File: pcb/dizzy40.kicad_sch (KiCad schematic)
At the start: 102 parts, among them U1 ATmega32U2-A, U2 SRV05-4, X1 Crystal_GND24_Small

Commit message: finalize fab version
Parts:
- RGB1, RGB2, RGB3, RGB4, RGB5, RGB6, RGB7, RGB8: LCSC (none) -> C965556
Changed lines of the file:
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@@
       (effects (font (size 1.27 1.27)) (justify left top) hide)
+    )
+    (property "LCSC" "C965556" (id 4) (at 152.4 139.7 0)
+      (effects (font (size 1.27 1.27)) hide)
     )
     (pin "1")
@@
       (effects (font (size 1.27 1.27)) (justify left top) hide)
     )
+    (property "LCSC" "C965556" (id 4) (at 228.6 139.7 0)
+      (effects (font (size 1.27 1.27)) hide)
+    )
     (pin "1")
     (pin "2")
@@
       (effects (font (size 1.27 1.27)) (justify left top) hide)
     )
+    (property "LCSC" "C965556" (id 4) (at 213.36 139.7 0)
+      (effects (font (size 1.27 1.27)) hide)
+    )
     (pin "1")
     (pin "2")
@@
       (effects (font (size 1.27 1.27)) (justify left top) hide)
     )
+    (property "LCSC" "C965556" (id 4) (at 167.64 139.7 0)
+      (effects (font (size 1.27 1.27)) hide)
+    )
     (pin "1")
     (pin "2")
@@
       (effects (font (size 1.27 1.27)) (justify left top) hide)
     )
+    (property "LCSC" "C965556" (id 4) (at 243.84 139.7 0)
+      (effects (font (size 1.27 1.27)) hide)
+    )
     (pin "1")
     (pin "2")
@@
       (effects (font (size 1.27 1.27)) (justify left top) hide)
     )
+    (property "LCSC" "C965556" (id 4) (at 182.88 139.7 0)
+      (effects (font (size 1.27 1.27)) hide)
+    )
     (pin "1")
     (pin "2")
@@
       (effects (font (size 1.27 1.27)) (justify left top) hide)
     )
+    (property "LCSC" "C965556" (id 4) (at 198.12 139.7 0)
+      (effects (font (size 1.27 1.27)) hide)
+    )
     (pin "1")
     (pin "2")
@@
       (effects (font (size 1.27 1.27)) (justify left top) hide)
     )
-    (pin "1")
+    (property "LCSC" "C965556" (id 4) (at 259.08 139.7 0)
+      (effects (font (size 1.27 1.27)) hide)
+    )
+    (pin "1")

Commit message: update LED part number
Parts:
- RGB1, RGB2, RGB3, RGB4, RGB5, RGB6, RGB7, RGB8: LCSC C965556 -> C965555
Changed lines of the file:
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@@
       (effects (font (size 1.27 1.27)) (justify left top) hide)
     )
-    (property "LCSC" "C965556" (id 4) (at 152.4 139.7 0)
+    (property "LCSC" "C965555" (id 4) (at 152.4 139.7 0)
       (effects (font (size 1.27 1.27)) hide)
     )
@@
       (effects (font (size 1.27 1.27)) (justify left top) hide)
     )
-    (property "LCSC" "C965556" (id 4) (at 228.6 139.7 0)
+    (property "LCSC" "C965555" (id 4) (at 228.6 139.7 0)
       (effects (font (size 1.27 1.27)) hide)
     )
@@
       (effects (font (size 1.27 1.27)) (justify left top) hide)
     )
-    (property "LCSC" "C965556" (id 4) (at 213.36 139.7 0)
+    (property "LCSC" "C965555" (id 4) (at 213.36 139.7 0)
       (effects (font (size 1.27 1.27)) hide)
     )
@@
       (effects (font (size 1.27 1.27)) (justify left top) hide)
     )
-    (property "LCSC" "C965556" (id 4) (at 167.64 139.7 0)
+    (property "LCSC" "C965555" (id 4) (at 167.64 139.7 0)
       (effects (font (size 1.27 1.27)) hide)
     )
@@
       (effects (font (size 1.27 1.27)) (justify left top) hide)
     )
-    (property "LCSC" "C965556" (id 4) (at 243.84 139.7 0)
+    (property "LCSC" "C965555" (id 4) (at 243.84 139.7 0)
       (effects (font (size 1.27 1.27)) hide)
     )
@@
       (effects (font (size 1.27 1.27)) (justify left top) hide)
     )
-    (property "LCSC" "C965556" (id 4) (at 182.88 139.7 0)
+    (property "LCSC" "C965555" (id 4) (at 182.88 139.7 0)
       (effects (font (size 1.27 1.27)) hide)
     )
@@
       (effects (font (size 1.27 1.27)) (justify left top) hide)
     )
-    (property "LCSC" "C965556" (id 4) (at 198.12 139.7 0)
+    (property "LCSC" "C965555" (id 4) (at 198.12 139.7 0)
       (effects (font (size 1.27 1.27)) hide)
     )
@@
       (effects (font (size 1.27 1.27)) (justify left top) hide)
     )
-    (property "LCSC" "C965556" (id 4) (at 259.08 139.7 0)
-      (effects (font (size 1.27 1.27)) hide)
-    )
+    (property "LCSC" "C965555" (id 4) (at 259.08 139.7 0)
+      (effects (font (size 1.27 1.27)) hide)
+    )

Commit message: outline for updated project
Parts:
- removed C1: 10uF, Capacitor_SMD:C_0805_2012Metric, symbol Device:C_Small
- removed C2, C3: 0.1uF, Capacitor_SMD:C_0805_2012Metric, symbol Device:C_Small
- removed C4, C5: 22pF, Capacitor_SMD:C_0805_2012Metric, symbol Device:C_Small
- removed C6: 1uF, Capacitor_SMD:C_0805_2012Metric, symbol Device:C_Small
- removed F1: Polyfuse_Small, Fuse:Fuse_1206_3216Metric, symbol Device:Polyfuse_Small
- removed R1, R2: 5.1k, Resistor_SMD:R_0805_2012Metric, symbol Device:R_Small
- removed R3, R4: 22, Resistor_SMD:R_0805_2012Metric, symbol Device:R_Small
- removed R5, R6: 10k, Resistor_SMD:R_0805_2012Metric, symbol Device:R_Small
- removed RESET1: RESET, Connector_PinHeader_2.54mm:PinHeader_1x02_P2.54mm_Vertical, symbol Switch:SW_Push
- removed U1: ATmega32U2-A, Package_QFP:TQFP-32_7x7mm_P0.8mm, symbol MCU_Microchip_ATmega:ATmega32U2-A
- removed U2: SRV05-4, Package_TO_SOT_SMD:SOT-23-6, symbol Power_Protection:SRV05-4
- removed USB1: USB_C_Receptacle_USB2.0, Connector_USB:USB_C_Receptacle_HRO_TYPE-C-31-M-12, symbol Connector:USB_C_Receptacle_USB2.0
- removed X1: Crystal_GND24_Small, Crystal:Crystal_SMD_3225-4Pin_3.2x2.5mm, symbol Device:Crystal_GND24_Small
- added SW1, SW2: RotaryEncoder_Switch, symbol Device:RotaryEncoder_Switch
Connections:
- net GND: now also SW1.C, SW2.C
- new net ENC_ESC_L: SW1.A
- new net ENC_ESC_R: SW1.B
- new net ENC_SPC_L: SW2.A
- new net ENC_SPC_R: SW2.B
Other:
- added sheet MCU (../../Clacky40/pcb/rp2040/RP2040_tmp.kicad_sch)

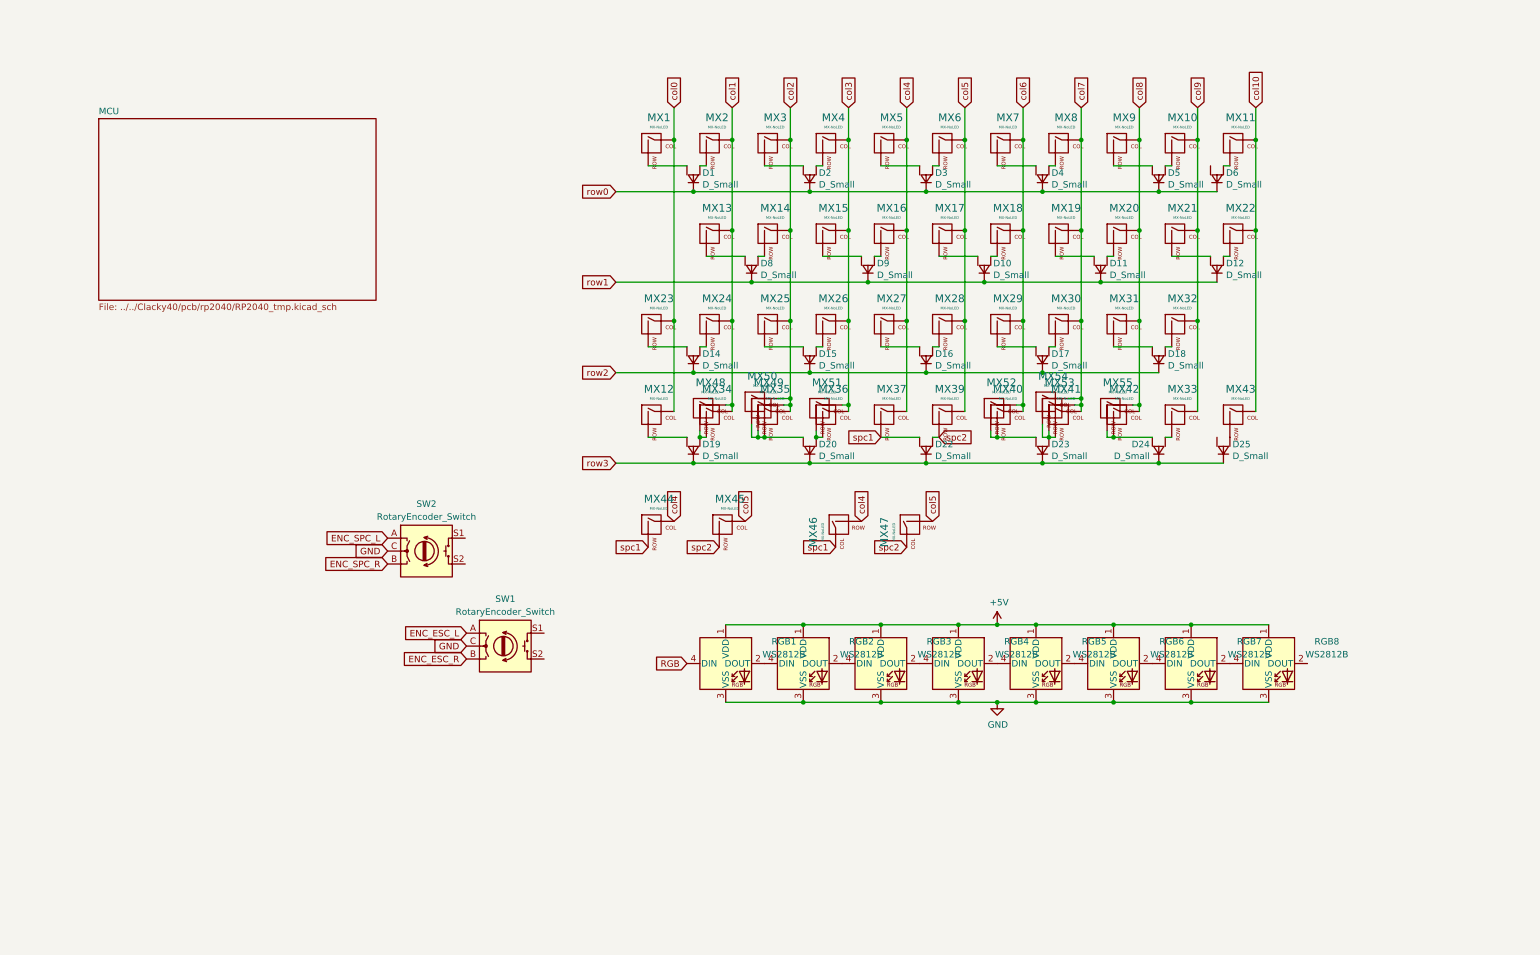
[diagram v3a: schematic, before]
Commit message: diode positioning done
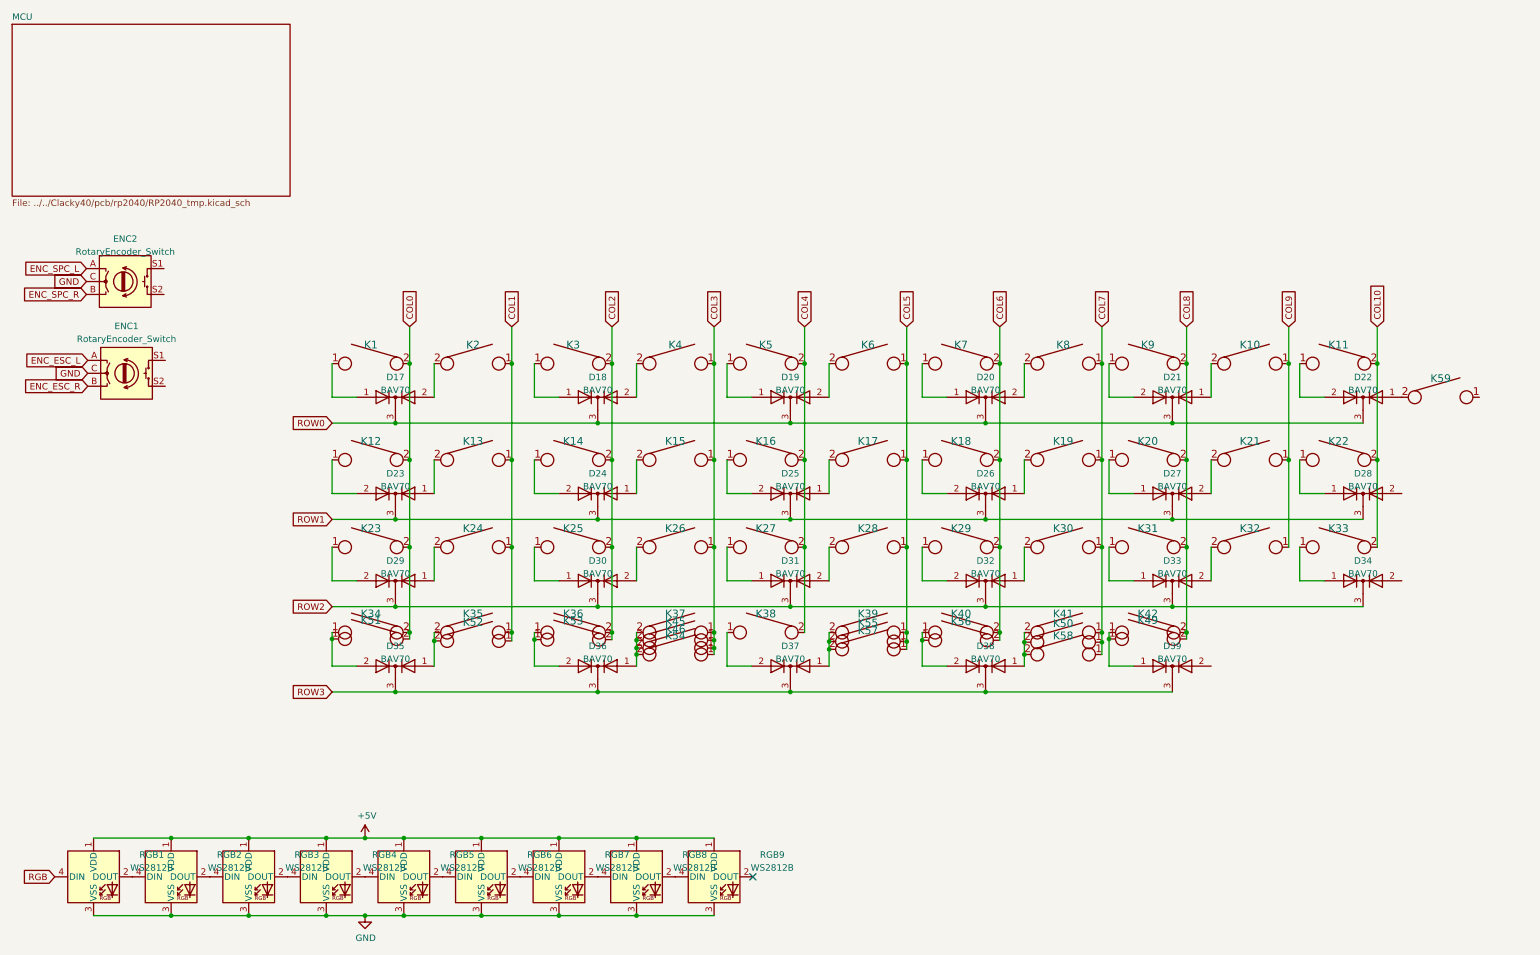
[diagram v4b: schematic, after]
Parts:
- removed D1, D10, D11, D12, D14, D15, D16, D17, D18, D19, D2, D20, D22, D23, D24, D25, D3, D4, D5, D6, D8, D9: D_Small, custom_parts:D_SOT-23_ANK_norm, symbol custom:D_AAK_Small
- removed MX1, MX10, MX11, MX13, MX14, MX15, MX16, MX17, MX18, MX19, MX2, MX20, MX21, MX24, MX25, MX26, MX27, MX28, MX29, MX3, MX30, MX31, MX32, MX35, MX4, MX41, MX43, MX5, MX50, MX51, MX52, MX54, MX6, MX7, MX8, MX9: MX-NoLED, MX_Only:MXOnly-1U-NoLED, symbol MX_Alps_Hybrid:MX-NoLED
- removed MX12, MX33, MX34, MX36, MX40, MX42, MX49, MX53: MX-NoLED, MX_Only:MXOnly-1.25U-NoLED, symbol MX_Alps_Hybrid:MX-NoLED
- removed MX22, MX23: MX-NoLED, MX_Only:MXOnly-1.75U-NoLED, symbol MX_Alps_Hybrid:MX-NoLED
- removed MX37: MX-NoLED, MX_Only:MXOnly-3U-ReversedStabilizers-NoLED, symbol MX_Alps_Hybrid:MX-NoLED
- removed MX39: MX-NoLED, MX_Only:MXOnly-2U-ReversedStabilizers-NoLED, symbol MX_Alps_Hybrid:MX-NoLED
- removed MX44, MX47: MX-NoLED, MX_Only:MXOnly-2.75U-ReversedStabilizers-NoLED, symbol MX_Alps_Hybrid:MX-NoLED
- removed MX45, MX46: MX-NoLED, MX_Only:MXOnly-2.25U-ReversedStabilizers-NoLED, symbol MX_Alps_Hybrid:MX-NoLED
- removed MX48, MX55: MX-NoLED, MX_Only:MXOnly-1.5U-NoLED, symbol MX_Alps_Hybrid:MX-NoLED
- added D17, D18, D19, D20, D21, D22, D23, D24, D25, D26, D27, D28, D29, D30, D31, D32, D33, D34, D35, D36, D37, D38, D39: BAV70, Package_TO_SOT_SMD:SOT-23, symbol Diode:BAV70
- added K1, K10, K11, K12, K13, K14, K15, K16, K17, K18, K19, K2, K20, K21, K22, K23, K24, K25, K26, K27, K28, K29, K3, K30, K31, K32, K33, K34, K35, K36, K37, K38, K39, K4, K40, K41, K42, K45, K46, K49, K5, K50, K51, K52, K53, K54, K55, K56, K57, K58, K59, K6, K7, K8, K9: KEYSW, marbastlib-mx:SW_MX_1u, symbol keyboard_parts:KEYSW
- added RGB9: WS2812B, kbd:LED_WS2812B-PLCC4, symbol LED:WS2812B
- ENC1: renamed from SW1; footprint (none) -> Keebio-Parts:RotaryEncoder_Alps_EC11E-Switch_Vertical_H20mm
- ENC2: renamed from SW2; footprint (none) -> Keebio-Parts:RotaryEncoder_Alps_EC11E-Switch_Vertical_H20mm
- RGB1, RGB2, RGB3, RGB4, RGB5, RGB6, RGB7, RGB8: footprint custom_parts:WS2812-2020 -> kbd:LED_WS2812B-PLCC4
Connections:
- net +5V: now also RGB9.1 (VDD)
- net GND: now also RGB9.3 (VSS)
- net at RGB8.2 (DOUT): now also RGB9.4 (DIN)
- new net: D29.1 (A), K24.2
- new net: D29.2 (A), K23.1
- new net: D24.2 (A), K14.1
- new net: D18.1 (A), K3.1
- new net: D32.1 (A), K30.2
- new net: D32.2 (A), K29.1
- new net: D31.2 (A), K28.2
- new net: D19.1 (A), K5.1
- new net: D39.1 (A), K42.1, K49.1
- new net: D36.1 (A), K37.2, K45.2, K46.2, K54.2
- new net: D36.2 (A), K36.1, K53.1
- new net: D38.1 (A), K41.2, K50.2, K58.2
- new net: D38.2 (A), K40.1, K56.1
- new net: D33.2 (A), K32.2
- new net: D25.2 (A), K16.1
- new net: D17.2 (A), K2.2
- new net: D19.2 (A), K6.2
- new net: D20.1 (A), K7.1
- new net: D20.2 (A), K8.2
- new net: D35.1 (A), K35.2, K52.2
- new net: D23.1 (A), K13.2
- new net: D23.2 (A), K12.1
- new net: D24.1 (A), K15.2
- new net: D26.2 (A), K18.1
- new net: D35.2 (A), K34.1, K51.1
- new net: D37.1 (A), K39.2, K55.2, K57.2
- new net: D30.1 (A), K25.1
- new net: D18.2 (A), K4.2
- new net: D28.1 (A), K22.1
- new net: D22.1 (A), K59.2
- new net: D22.2 (A), K11.1
- new net: D17.1 (A), K1.1
- new net: D27.2 (A), K21.2
- new net: D34.1 (A), K33.1
- new net: D33.1 (A), K31.1
- new net: D26.1 (A), K19.2
- new net: D25.1 (A), K17.2
- new net: D21.2 (A), K9.1
- new net: D21.1 (A), K10.2
- new net: D37.2 (A), K38.1
- new net: D31.1 (A), K27.1
- new net: D30.2 (A), K26.2
- new net: D27.1 (A), K20.1
- new net COL0: K1.2, K12.2, K23.2, K34.2, K51.2
- new net COL1: K13.1, K2.1, K24.1, K35.1, K52.1
- new net COL10: K11.2, K22.2, K33.2
- new net COL2: K14.2, K25.2, K3.2, K36.2, K53.2
- new net COL3: K15.1, K26.1, K37.1, K4.1, K45.1, K46.1, K54.1
- new net COL4: K16.2, K27.2, K38.2, K5.2
- new net COL5: K17.1, K28.1, K39.1, K55.1, K57.1, K6.1
- new net COL6: K18.2, K29.2, K40.2, K56.2, K7.2
- new net COL7: K19.1, K30.1, K41.1, K50.1, K58.1, K8.1
- new net COL8: K20.2, K31.2, K42.2, K49.2, K9.2
- new net COL9: K10.1, K21.1, K32.1
- new net ROW0: D17.3 (K), D18.3 (K), D19.3 (K), D20.3 (K), D21.3 (K), D22.3 (K)
- new net ROW1: D23.3 (K), D24.3 (K), D25.3 (K), D26.3 (K), D27.3 (K), D28.3 (K)
- new net ROW2: D29.3 (K), D30.3 (K), D31.3 (K), D32.3 (K), D33.3 (K), D34.3 (K)
- new net ROW3: D35.3 (K), D36.3 (K), D37.3 (K), D38.3 (K), D39.3 (K)
- no-connect marks 0 -> 1
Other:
- moved on the sheet: ENC1, ENC2, RGB1, RGB2, RGB3, RGB4, RGB5, RGB6, RGB7, RGB8

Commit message: finalized routing, placement of components
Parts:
- added J3, J5, J6, J7, J8: Screw_Terminal_01x02, marbastlib-mx:STAB_MX_P_2u, symbol Connector:Screw_Terminal_01x02
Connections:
- net COL0: now also ENC1.S2
- net COL4: now also ENC2.S2
- net GND: now also J3.1 (Pin_1), J3.2 (Pin_2), J5.1 (Pin_1), J5.2 (Pin_2), J6.1 (Pin_1), J6.2 (Pin_2), J7.1 (Pin_1), J7.2 (Pin_2), J8.1 (Pin_1), J8.2 (Pin_2)
- net ENC_ROW_TOP: now reaches ENC1.S1
- net ENC_ROW_TOP: now also D17.1 (A), K1.1
- net ENC_ROW_MID: now reaches ENC2.S1
- net ENC_ROW_MID: now also D37.2 (A), K38.1
- net COL11: now reaches K59.1
